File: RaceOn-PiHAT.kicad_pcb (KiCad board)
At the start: 2 copper layers, 65 x 56.5 mm, 20 parts, among them J1 Conn_01x02, J2 Battery, J3 Servo_motor, J4 Conn_02x20_Odd_Even, J5 Accelerometer_standard, Q3 SQJA37EP1

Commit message: Included all parts in the schematic
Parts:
- J4: moved to B.Cu
- moved J4 2.50 mm to (128.0, 71.5)
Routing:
- net GPIO6: track 0.00 -> 120.1 mm, vias 0 -> 1
- net GPIO12: track 120.1 -> 0.00 mm, vias 1 -> 0
- net Net-(J4-Pad17): track 0.00 -> 30.1 mm, vias 0 -> 2
- net GPIO24: track 30.1 -> 0.00 mm, vias 2 -> 0
- net Net-(J4-Pad11): track 0.00 -> 17.3 mm, vias 0 -> 2
- net GPIO18: track 17.3 -> 0.00 mm, vias 2 -> 0
- net Net-(J4-Pad15): track 0.00 -> 15.8 mm, vias 0 -> 1
- net GPIO23: track 25.9 -> 10.1 mm, vias 2 -> 1
- net Net-(J4-Pad23): track 0.00 -> 6.73 mm
- net GPIO8: track 21.2 -> 14.5 mm
- net Net-(J4-Pad26): track 0.00 -> 6.52 mm
- net Net-(J4-Pad35): track 0.00 -> 5.51 mm
- net GPIO16: track 24.1 -> 18.5 mm
- net GPIO21: track 11.4 -> 7.90 mm
- net GND: track 95.3 -> 92.3 mm
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
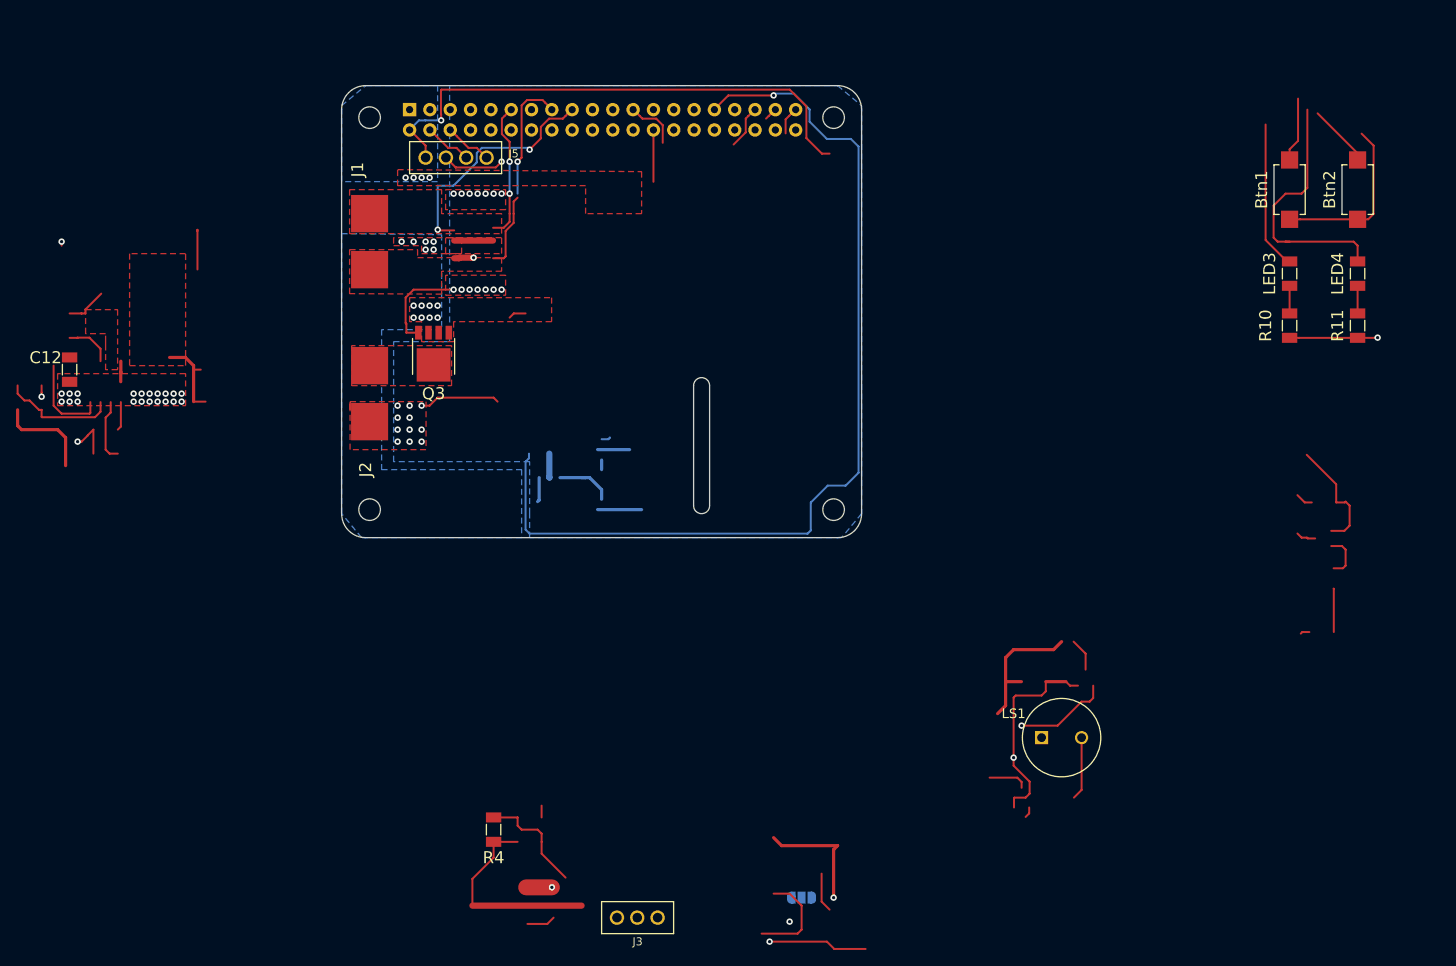
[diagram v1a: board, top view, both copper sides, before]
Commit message: Add footprints for all parts
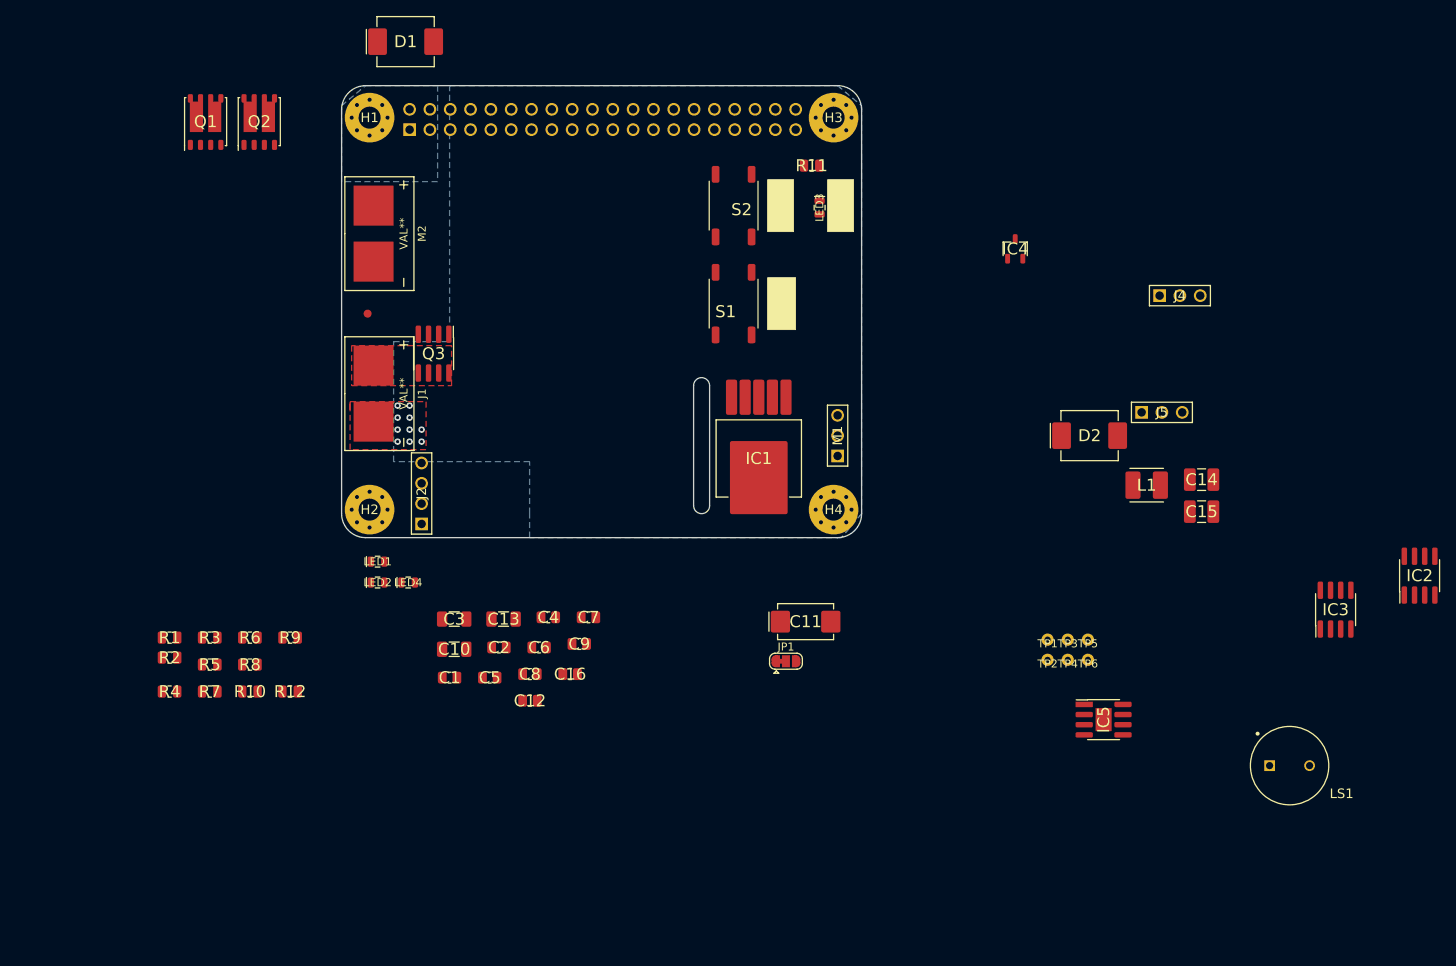
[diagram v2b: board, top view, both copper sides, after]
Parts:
- removed Btn2: PTS636, library_express_pro:PTS636
- removed the J3 at (156.5, 172.5)
- added C1: 100nF, Race On:CAPC200X125X95L45M, F.Cu at (133.0, 142.5)
- added C10: 4.7uF, Race On:CAPC320X160X180L50M, F.Cu at (133.6, 138.9)
- added C11: 100uF, Race On:CAPPM730X435X310L135X240L, F.Cu at (177.5, 135.5)
- added C13: 4.7uF, Race On:CAPC320X160X180L50M, F.Cu at (139.7, 135.2)
- added C14: 47uF, Race On:CAPC320X250X270L60M, F.Cu at (227.0, 117.8)
- added C15: 47uF, Race On:CAPC320X250X270L60M, F.Cu at (227.0, 121.8)
- added C16: 47nF, Race On:CAPC200X125X95L45M, F.Cu at (148.1, 142.1)
- added C2: 47nF, Race On:CAPC200X125X95L45M, F.Cu at (139.2, 138.7)
- added C3: 4.7uF, Race On:CAPC320X160X180L50M, F.Cu at (133.6, 135.2)
- added C4: 1uF, Race On:CAPC200X125X95L45M, F.Cu at (145.3, 135.0)
- added C5: 27nF, Race On:CAPC200X125X95L45M, F.Cu at (138.0, 142.5)
- added C6: 100nF, Race On:CAPC200X125X95L45M, F.Cu at (144.2, 138.7)
- added C7: 47nF, Race On:CAPC200X125X95L45M, F.Cu at (150.4, 135.0)
- added C8: 1uF, Race On:CAPC200X125X95L45M, F.Cu at (143.0, 142.1)
- added C9: 1uF, Race On:CAPC200X125X95L45M, F.Cu at (149.2, 138.3)
- added D1: D_Schottky, Race On:DIOM795X590X261L117X305M, F.Cu at (127.5, 63.0)
- added D2: D_Schottky, Race On:DIOM795X590X261L117X305M, F.Cu at (213.0, 112.2)
- added FID1: Fiducial, Race On:FID1M3, F.Cu at (122.8, 97.0)
- added IC1: MIC29302WU, Race On:DPAK6P67_587X190L89X29T300X275M, F.Cu at (171.6, 113.6)
- added IC2: NCP5901B, Race On:SOIC8P127_490X600X175L83X42M, F.Cu at (254.2, 129.8)
- added IC3: NCP5901B, Race On:SOIC8P127_490X600X175L83X42M, F.Cu at (243.8, 134.0)
- added IC4: BD48K60G, Race On:SOT23-3P95_280X125L45X40M, F.Cu at (203.7, 88.9)
- added IC5: LMR14030, Race On:SOIC9P127_490X600X170L83X41T287X202M, F.Cu at (214.8, 147.8)
- added J4: Encoder Left, Race On:HDRV3W64P254_3X1_762X254H854, F.Cu at (221.8, 94.8)
- added L1: 1uH, Race On:INDM400X400X200L95X310M, F.Cu at (220.1, 118.4)
- added LED1: RED, Race On:LEDC197X125X85L45L, F.Cu at (124.0, 128.0)
- added LED2: GREEN, Race On:LEDC197X125X85L45L, F.Cu at (124.0, 130.6)
- added M1: Servo, Race On:HDRV3W64P254_3X1_762X254H854, F.Cu at (181.5, 114.8)
- added M2: Mabuchi 540, Race On:CON2P, F.Cu at (126.0, 87.0)
- added Q1: Si7288DP, Race On:ICSOFL8P127_515X615X112L61X42M, F.Cu at (102.5, 73.0)
- added Q2: Si7288DP, Race On:ICSOFL8P127_515X615X112L61X42M, F.Cu at (109.2, 73.0)
- added R1: 46.4k, Race On:RESC200X127X65L40M, F.Cu at (98.0, 137.5)
- added R12: 4.7k, Race On:RESC200X127X65L40M, F.Cu at (113.1, 144.2)
- added R2: 12.1k, Race On:RESC200X127X65L40M, F.Cu at (98.0, 140.0)
- added R3: 12.1k, Race On:RESC200X127X65L40M, F.Cu at (103.0, 137.5)
- added R5: 4.7k, Race On:RESC200X127X65L40M, F.Cu at (103.0, 140.9)
- added R6: 12.1k, Race On:RESC200X127X65L40M, F.Cu at (108.0, 137.5)
- added R7: 4.7k, Race On:RESC200X127X65L40M, F.Cu at (103.0, 144.2)
- added R8: 68.1k, Race On:RESC200X127X65L40M, F.Cu at (108.0, 140.9)
- added R9: 12.1k, Race On:RESC200X127X65L40M, F.Cu at (113.1, 137.5)
- added S2: RIGHT, Race On:BTN4P450_600X900X350L83X70M, F.Cu at (168.5, 83.5)
- added TP1: TestPoint, Race On:TESTPOINT, F.Cu at (207.8, 137.8)
- added TP2: TestPoint, Race On:TESTPOINT, F.Cu at (207.8, 140.3)
- added TP3: TestPoint, Race On:TESTPOINT, F.Cu at (210.3, 137.8)
- added TP4: TestPoint, Race On:TESTPOINT, F.Cu at (210.3, 140.3)
- added TP5: TestPoint, Race On:TESTPOINT, F.Cu at (212.8, 137.8)
- added TP6: TestPoint, Race On:TESTPOINT, F.Cu at (212.8, 140.3)
- C12: value 10uF -> 100nF; footprint library_express_pro:RLC_EIA_3216 -> Race On:CAPC200X125X95L45M
- H1, H2, H3, H4: footprint MountingHole:MountingHole_2.7mm_M2.5 -> Race On:MTGP620H275V8H50
- J1: value Conn_01x02 -> Battery; footprint library_express_pro:Connector_pads -> Race On:CON2P
- J2: value Battery -> Accelerometer; footprint library_express_pro:Connector_pads -> Race On:HDRV4W64P254_4X1_1016X254H854
- J3: renamed from J4; value Conn_02x20_Odd_Even -> Pi Connector; footprint library_express_pro:RasPi_Header_0.9 -> Race On:RHDRV40W64P254_20X2_5120X500H850
- J5: value Accelerometer_standard -> Encoder Right; footprint library_express_pro:Accelerometer_standard -> Race On:HDRV3W64P254_3X1_762X254H854
- JP1: value SolderJumper_3_Bridged12 -> SolderJumper; footprint Jumper:SolderJumper-3_P1.3mm_Open_RoundedPad1.0x1.5mm_NumberLabels -> Race On:SJ3B12P10X15; moved to F.Cu
- LED3: value 599-0210-007F -> RED; footprint library_express_pro:RLC_EIA_3216 -> Race On:LEDC197X125X85L45L
- LED4: value 599-0210-007F -> GREEN; footprint library_express_pro:RLC_EIA_3216 -> Race On:LEDC197X125X85L45L
- LS1: footprint library_express_pro:Buzzer_AI1027TWT5V2R -> Race On:LSP500W60D980H500
- Q3: footprint library_express_pro:SO-8L -> Race On:SOIC8P127_490X600X175L83X42M-TRANZISTOR
- R10: value 2.2k -> 12.1k; footprint library_express_pro:RLC_EIA_3216 -> Race On:RESC200X127X65L40M
- R11: value 6.8k -> 4.7k; footprint library_express_pro:RLC_EIA_3216 -> Race On:RESC200X127X65L40M
- R4: value 22.1k -> 12.1k; footprint library_express_pro:RLC_EIA_3216 -> Race On:RESC200X127X65L40M
- S1: renamed from Btn1; value PTS636 -> LEFT; footprint library_express_pro:PTS636 -> Race On:BTN4P450_600X900X350L83X70M
- moved R10 137.8 mm to (108.0, 144.2), turned to 0 degrees
- moved LED4 124.8 mm to (127.8, 130.6), turned to 0 degrees
- moved J5 95.0 mm to (219.5, 109.3)
- moved R11 71.1 mm to (178.2, 78.5), turned to 180 degrees
- moved S1 70.9 mm to (168.5, 95.8), turned to 180 degrees
- moved C12 70.9 mm to (143.0, 145.4), turned to 0 degrees
- moved LED3 59.3 mm to (179.2, 83.8), turned to 270 degrees
- moved R4 44.0 mm to (98.0, 144.2), turned to 0 degrees
- moved JP1 29.6 mm to (175.0, 140.4)
- moved LS1 28.7 mm to (238.0, 153.5)
- moved J1 19.2 mm to (126.0, 107.0)
- moved J2 17.5 mm to (129.5, 123.3), turned to 90 degrees
- moved J3 2.50 mm to (128.0, 74.0)
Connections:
- net GPIO25 renamed BCM9
- net GPIO8 renamed BCM11
- net Net-(J4-Pad11) renamed BCM18
- net Net-(J4-Pad21) renamed BCM25
- net Net-(J4-Pad23) renamed BCM8
- net Net-(J4-Pad27) renamed BCM1
- net Net-(J4-Pad28) renamed BCM0
- net Net-(J4-Pad8) renamed BCM4
- net Net-(J4-Pad9) renamed BCM15
- C12 pad 1: GND -> Net-(C12-Pad1)
- C12 pad 2: +BATT -> Net-(C12-Pad2)
- J1 pad 2: Net-(J1-Pad2) -> GND
- J2 pad 1: Net-(J2-Pad1) -> +3V3
- J3 pad 1: +3V3 -> Net-(D1-Pad1)
- J3 pad 10: Net-(J4-Pad10) -> GND
- J3 pad 12: GPIO18 -> BCM17
- J3 pad 13: Net-(J4-Pad13) -> GND
- J3 pad 14: GND -> BCM27
- J3 pad 15: Net-(J4-Pad15) -> BCM23
- J3 pad 16: GPIO23 -> BCM22
- J3 pad 17: Net-(J4-Pad17) -> BCM24
- J3 pad 18: GPIO24 -> +3V3
- J3 pad 19: Net-(J4-Pad19) -> GND
- J3 pad 2: +5V -> +3V3
- J3 pad 20: GND -> BCM10
- J3 pad 25: GND -> BCM7
- J3 pad 26: Net-(J4-Pad26) -> GND
- J3 pad 29: GPIO5 -> GND
- J3 pad 3: SDA -> Net-(D1-Pad1)
- J3 pad 30: GND -> BCM5
- J3 pad 31: GPIO6 -> BCM12
- J3 pad 32: GPIO12 -> BCM6
- J3 pad 33: GPIO13 -> GND
- J3 pad 34: GND -> BCM13
- J3 pad 35: Net-(J4-Pad35) -> BCM16
- J3 pad 36: GPIO16 -> BCM19
- J3 pad 37: GPIO26 -> BCM20
- J3 pad 38: GPIO20 -> BCM26
- J3 pad 39: GND -> BCM21
- J3 pad 4: +5V -> BCM2
- J3 pad 40: GPIO21 -> GND
- J3 pad 5: SCL -> GND
- J3 pad 6: GND -> BCM3
- J3 pad 7: GND -> BCM14
- J5 pad 3: SDA -> BCM24
- JP1 pad 1: Vservo -> Net-(C3-Pad2)
- LED3 pad 2: GPIO16 -> BCM16
- LED4 pad 2: GPIO26 -> BCM26
- Q3 pad 1: Net-(J2-Pad1) -> Net-(J1-Pad1)
- R10 pad 2: Net-(LED3-Pad1) -> VFB
- R11 pad 1: GND -> Net-(LED3-Pad1)
- R11 pad 2: Net-(LED4-Pad1) -> GND
- R4 pad 1: Net-(IC1-Pad5) -> GND
- R4 pad 2: GND -> Net-(IC1-Pad5)
- S1 pad 1: +3V3 -> BCM5
- S1 pad 2: GPIO20 -> +3V3
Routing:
- net GPIO6: track 120.1 -> 0.00 mm, vias 1 -> 0
- net GND: track 92.3 -> 0.00 mm, vias 50 -> 10
- net +3V3: track 88.9 -> 0.00 mm, vias 1 -> 0
- net +5V: track 67.6 -> 0.00 mm, vias 5 -> 0
- net GPIO26: track 34.0 -> 0.00 mm
- net +BATT: track 30.6 -> 0.00 mm, vias 10 -> 0
- net Net-(J4-Pad17): track 30.1 -> 0.00 mm, vias 2 -> 0
- net Net-(IC1-Pad1): track 27.2 -> 0.00 mm, vias 1 -> 0
- net Net-(IC1-Pad5): track 25.7 -> 0.00 mm
- net Net-(IC4-Pad2): track 22.5 -> 0.00 mm
- net GPIO16: track 18.5 -> 0.00 mm
- net BCM18: track 17.3 -> 0.00 mm, vias 2 -> 0
- net Net-(IC2-Pad1): track 15.9 -> 0.00 mm
- net Net-(J4-Pad15): track 15.8 -> 0.00 mm, vias 1 -> 0
- net BCM11: track 14.5 -> 0.00 mm
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- removed copper zone on F.Cu, net +5V
- removed copper zone on B.Cu, net +BATT
- removed copper zone on F.Cu, net +BATT
- removed copper zone on F.Cu, net Net-(C4-Pad1)
- removed copper zone on F.Cu, net Net-(J1-Pad2)
- removed copper zone on F.Cu, net Net-(J2-Pad1)
- removed copper zone on F.Cu, net Vbat

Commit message: Ordered from Seeed PCBA
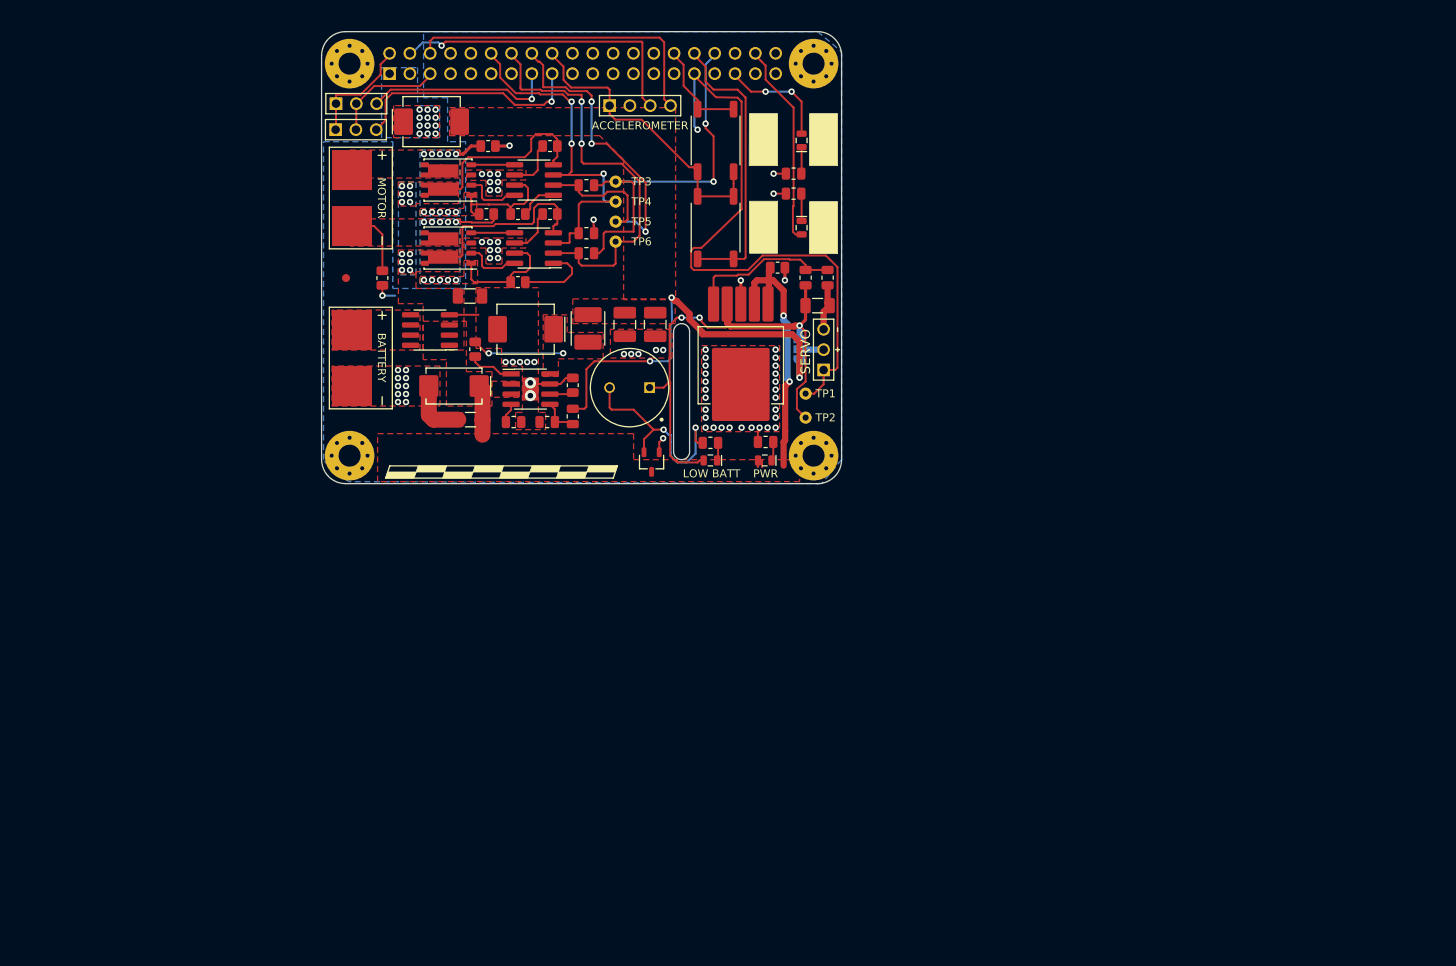
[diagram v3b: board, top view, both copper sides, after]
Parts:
- added LOGO1: RACEON-LOGO, Race On:RACEON-LOGO, F.Cu at (140.2, 114.0)
- J1: value Battery -> BATTERY
- J2: value Accelerometer -> ACCELEROMETER
- JP1: moved to B.Cu
- M1: value Servo -> SERVO
- M2: value Mabuchi 540 -> MOTOR
- moved IC2 121.2 mm to (143.6, 80.3), turned to 90 degrees
- moved IC3 109.9 mm to (143.6, 88.8), turned to 90 degrees
- moved J5 106.8 mm to (118.8, 74.0)
- moved J4 105.7 mm to (118.8, 70.8)
- moved R4 97.2 mm to (180.2, 92.5), turned to 90 degrees
- moved LS1 95.1 mm to (155.5, 106.2), turned to 180 degrees
- moved R1 91.4 mm to (177.5, 92.5), turned to 90 degrees
- moved R12 88.5 mm to (176.0, 82.0)
- moved IC5 82.7 mm to (143.1, 106.4)
- moved TP4 80.5 mm to (153.8, 83.0)
- moved TP3 80.4 mm to (153.8, 80.5)
- moved TP6 78.9 mm to (153.8, 88.0)
- moved TP5 78.8 mm to (153.8, 85.5)
- moved R2 78.7 mm to (150.1, 81.0), turned to 180 degrees
- moved R7 76.2 mm to (172.5, 113.0)
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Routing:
- net +BATT: track 0.00 -> 88.9 mm, vias 0 -> 14
- net BCM12: track 0.00 -> 76.8 mm, vias 0 -> 1
- net GND: track 0.00 -> 67.9 mm, vias 10 -> 71
- net Net-(C3-Pad2): track 0.00 -> 64.0 mm, vias 0 -> 3
- net BCM22: track 0.00 -> 51.7 mm, vias 0 -> 3
- net +3V3: track 0.00 -> 51.5 mm
- net BCM27: track 0.00 -> 51.3 mm, vias 0 -> 2
- net +5V: track 0.00 -> 50.9 mm, vias 0 -> 3
- net BCM13: track 0.00 -> 49.1 mm, vias 0 -> 2
- net BCM17: track 0.00 -> 46.6 mm, vias 0 -> 3
- net BCM3: track 0.00 -> 39.7 mm
- net BCM2: track 0.00 -> 38.4 mm, vias 0 -> 1
- net BCM6: track 0.00 -> 35.8 mm
- net BCM24: track 0.00 -> 29.4 mm, vias 0 -> 1
- net Net-(C5-Pad1): track 0.00 -> 28.7 mm, vias 0 -> 10
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- added copper zone on F.Cu, net +5V
- added copper zone on B.Cu, net +BATT
- added copper zone on F.Cu, net +BATT
- added copper zone on B.Cu, net Net-(C1-Pad1)
- added copper zone on F.Cu, net Net-(C1-Pad1)
- added copper zone on F.Cu, net Net-(C12-Pad1)
- added copper zone on B.Cu, net Net-(C5-Pad1)
- added copper zone on F.Cu, net Net-(C5-Pad1)
- added copper zone on B.Cu, net Net-(D1-Pad1)
- added copper zone on F.Cu, net Net-(D1-Pad1)
- removed copper zone on B.Cu, net +5V
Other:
- board text added: "LOW BATT"
- board text added: "PWR"
